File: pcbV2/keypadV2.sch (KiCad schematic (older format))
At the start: 74 parts, among them J1 Conn_01x02_Female, J2 USB_C_Receptacle, J3 Conn_01x03_Male, Q1 Q_NMOS_GSD, SW1 SW_Push, SW10 SW_Push, SW11 SW_Push, SW12 SW_Push, SW13 SW_SPDT, SW14 SW_Push, SW15 SW_Push, SW16 SW_Push, SW17 SW_DIP_x03, SW2 SW_Push, SW3 SW_Push, SW4 SW_Push, SW5 SW_Push, SW6 SW_Push, SW7 SW_Push, SW8 SW_Push, SW9 SW_Push, U1 Teensy4.0, U2 Waveshare_OLED_RGB

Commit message: .
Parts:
- added J6: Conn_01x03_Male, symbol Connector:Conn_01x03_Male
- J3: footprint Connector_PinHeader_2.00mm:PinHeader_1x03_P2.00mm_Vertical -> Connector_PinHeader_2.54mm:PinHeader_1x03_P2.54mm_Vertical
- R6: footprint (none) -> Resistor_SMD:R_1206_3216Metric_Pad1.42x1.75mm_HandSolder
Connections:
- net at D22.2 (DOUT): no longer D29.4 (DIN)
- new net RGB_UNDER: D29.4 (DIN), J6.2 (Pin_2)
- no-connect marks 45 -> 47
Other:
- moved on the sheet: C13, C14, C15, C16, D26, D27, D28, D29

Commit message: Start daughterboard
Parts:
- J6: footprint (none) -> Connector_PinSocket_2.54mm:PinSocket_1x03_P2.54mm_Vertical
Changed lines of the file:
@@
 F 0 "J6" H 8058 14631 50  0000 C CNN
 F 1 "Conn_01x03_Male" H 8058 14540 50  0000 C CNN
-F 2 "" H 7950 14350 50  0001 C CNN
+F 2 "Connector_PinSocket_2.54mm:PinSocket_1x03_P2.54mm_Vertical" H 7950 14350 50  0001 C CNN
 F 3 "~" H 7950 14350 50  0001 C CNN
 	1    7950 14350

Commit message: Updated schematic on mainboard, LEDs moved to daughter board
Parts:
- removed C1, C10, C11, C12, C2, C3, C4, C5, C6, C7, C8, C9: 1000uF, Capacitor_SMD:C_1206_3216Metric_Pad1.42x1.75mm_HandSolder, symbol Device:C
- removed D14, D15, D16, D17, D18, D19, D20, D21, D22, D23, D24, D25: WS2812B, LED_SMD:LED_WS2812B_PLCC4_5.0x5.0mm_P3.2mm, symbol LED:WS2812B
- removed R5: R_DIN, Resistor_SMD:R_1206_3216Metric_Pad1.42x1.75mm_HandSolder, symbol Device:R
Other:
- note added: "*Connect jumper to use 3.3V logic instead of the shifted 5V"
- note added: "Addressable RGBs"
- note added: "Keyboard Matrix"
- note added: "RGB Data Logic Level Shifter"
- note added: "RGB Daughter Board Connectors"
- note added: "Underglow RGB LEDs"
- note removed: "*Included extra 4 LEDs for underglow"
- note removed: "*Option to put 220-470ohm (close to DIN)"
- note removed: "*Use 3.3V logic instead of the shifted 5V"
- note removed: "Logic Level Shifter"
- note removed: "RGB Lighting"
- moved on the sheet: C13, C14, C15, C16, D13, D26, D27, D28, D29, J3, J6, Q1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

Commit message: Updated schematic to use seperate RGB Data pin for underglow LEDs
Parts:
- added H1, H2, H3, H4: MountingHole, MountingHole:MountingHole_3.2mm_M3, symbol Mechanical:MountingHole
- added Q2: Q_NMOS_GSD, Package_TO_SOT_SMD:SOT-23, symbol Device:Q_NMOS_GSD
- added R7: JUMPER, Resistor_SMD:R_1206_3216Metric_Pad1.42x1.75mm_HandSolder, symbol Device:R
- added R? (x2): 10K, Resistor_SMD:R_1206_3216Metric_Pad1.42x1.75mm_HandSolder, symbol Device:R
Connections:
- net +3V3: now also Q2.1 (G), R?.1
- net +5V: now also R?.1
- net BTN: now also U1.25 (18_A4_SDA0); no longer U1.21 (14_A0_TX3_SPDIF_OUT)
- net RGB_UNDER: now also Q2.3 (D), R7.1, R?.2; no longer J6.2 (Pin_2)
- net RGB_DATA renamed RGB_DATA1
- new net RGB_DATA2: Q2.2 (S), R7.2, R?.2, U1.21 (14_A0_TX3_SPDIF_OUT)
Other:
- note added: "*Empty connector used \nfor structural support"
- note added: "Mounting Holes"
- note added: "RGB Data Logic Level Shifter \n(Individual Backlighting)"
- note added: "RGB Data Logic Level Shifter \n(Underglow)"
- note removed: "RGB Data Logic Level Shifter"
- moved on the sheet: C13, C14, C15, C16, D26, D27, D28, D29, J3, J6

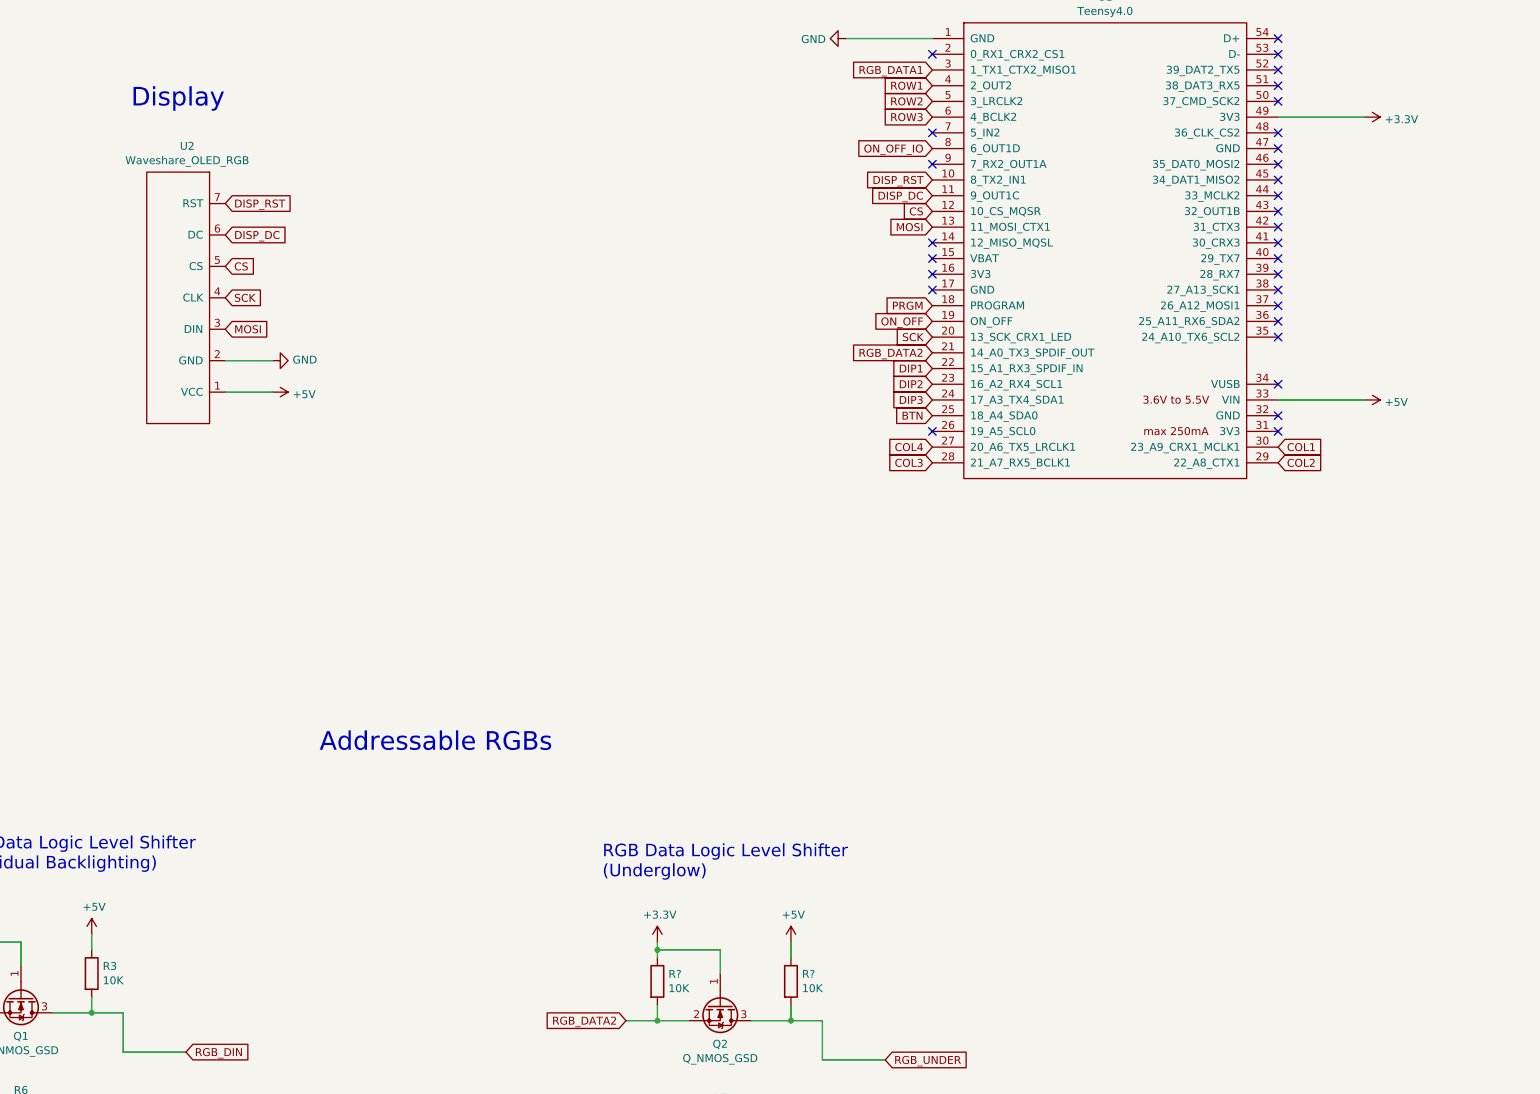
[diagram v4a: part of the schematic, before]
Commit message: 3.3V was on wrong pin on teens
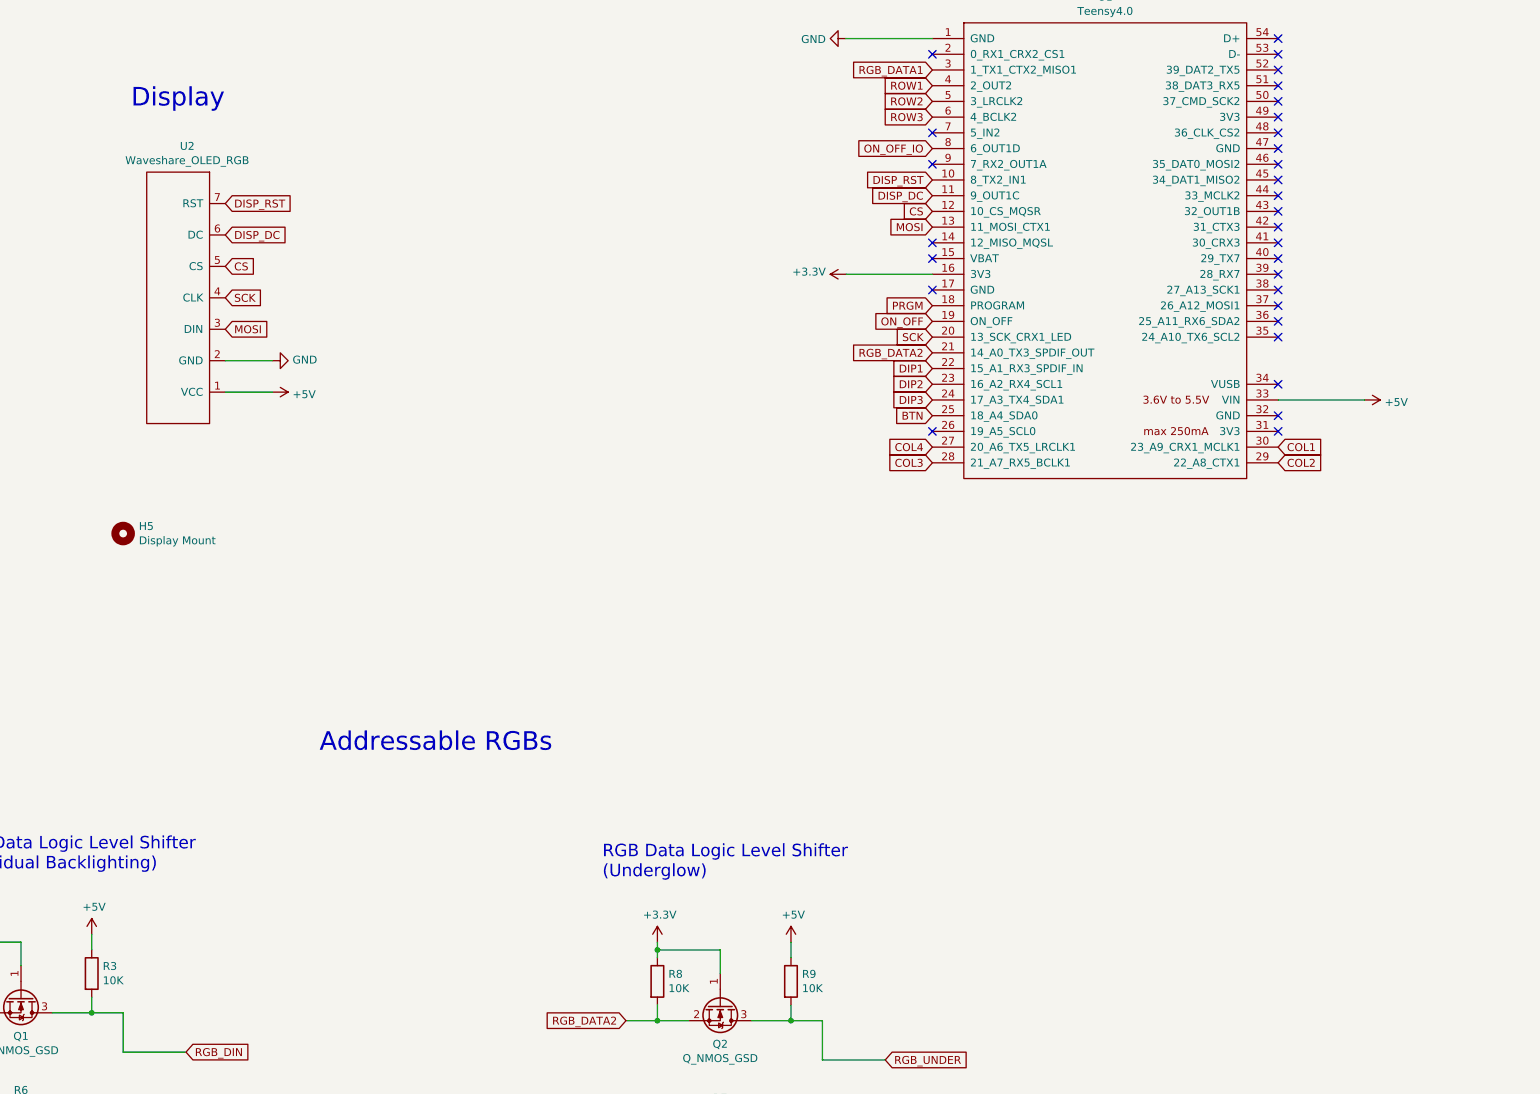
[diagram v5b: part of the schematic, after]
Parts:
- added H5: Display Mount, custom:Waveshare_LCD_mount V2, symbol Mechanical:MountingHole
- gave numbers to parts that had none: 2
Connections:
- net +3V3: now also U1.16 (3V3); no longer U1.49 (3V3)
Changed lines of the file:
@@
 L power:+3.3V #PWR0131
 U 1 1 5F108207
-P 11500 3550
-F 0 "#PWR0131" H 11500 3400 50  0001 C CNN
-F 1 "+3.3V" V 11515 3678 50  0000 L CNN
-F 2 "" H 11500 3550 50  0001 C CNN
-F 3 "" H 11500 3550 50  0001 C CNN
-	1    11500 3550
-	0    1    1    0
-$EndComp
-Wire Wire Line
-	11500 3550 10950 3550
+P 8200 4550
+F 0 "#PWR0131" H 8200 4400 50  0001 C CNN
+F 1 "+3.3V" V 8215 4678 50  0000 L CNN
+F 2 "" H 8200 4550 50  0001 C CNN
+F 3 "" H 8200 4550 50  0001 C CNN
+	1    8200 4550
+	0    -1   -1   0
+$EndComp
+Wire Wire Line
+	8200 4550 8750 4550
 Text GLabel 8750 4750 0    50   Input ~ 0
 PRGM
@@
 NoConn ~ 8750 4350
 NoConn ~ 8750 4450
-NoConn ~ 8750 4550
 NoConn ~ 8750 4650
 NoConn ~ 8750 5550
@@
 NoConn ~ 3000 11600
 $Comp
-L Device:R R?
+L Device:R R8
 U 1 1 5F102D2A
 P 7000 9050
-F 0 "R?" H 7070 9096 50  0000 L CNN
+F 0 "R8" H 7070 9096 50  0000 L CNN
 F 1 "10K" H 7070 9005 50  0000 L CNN
 F 2 "Resistor_SMD:R_1206_3216Metric_Pad1.42x1.75mm_HandSolder" V 6930 9050 50  0001 C CNN
@@
 $EndComp
 $Comp
-L Device:R R?
+L Device:R R9
 U 1 1 5F102D3F
 P 7850 9050
-F 0 "R?" H 7920 9096 50  0000 L CNN
+F 0 "R9" H 7920 9096 50  0000 L CNN
 F 1 "10K" H 7920 9005 50  0000 L CNN
 F 2 "Resistor_SMD:R_1206_3216Metric_Pad1.42x1.75mm_HandSolder" V 7780 9050 50  0001 C CNN
@@
 $EndComp
 $Comp
-L power:+3.3V #PWR?
+L power:+3.3V #PWR0101
 U 1 1 5F102D49
 P 7000 8800
-F 0 "#PWR?" H 7000 8650 50  0001 C CNN
+F 0 "#PWR0101" H 7000 8650 50  0001 C CNN
 F 1 "+3.3V" H 7015 8973 50  0000 C CNN
 F 2 "" H 7000 8800 50  0001 C CNN
@@
 $EndComp
 $Comp
-L power:+5V #PWR?
+L power:+5V #PWR0102
 U 1 1 5F102D53
 P 7850 8800
-F 0 "#PWR?" H 7850 8650 50  0001 C CNN
+F 0 "#PWR0102" H 7850 8650 50  0001 C CNN
 F 1 "+5V" H 7865 8973 50  0000 C CNN
 F 2 "" H 7850 8800 50  0001 C CNN
@@
 Text Notes 18300 6050 0    118  ~ 0
 Mounting Holes
+$Comp
+L Mechanical:MountingHole H5
+U 1 1 5F161619
+P 3600 6200
+F 0 "H5" H 3700 6246 50  0000 L CNN
+F 1 "Display Mount" H 3700 6155 50  0000 L CNN
+F 2 "custom:Waveshare_LCD_mount V2" H 3600 6200 50  0001 C CNN
+F 3 "~" H 3600 6200 50  0001 C CNN
+	1    3600 6200
+	1    0    0    -1
+$EndComp
+NoConn ~ 10950 3550
 $EndSCHEMATC

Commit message: Prototype 1 Code changes (#9)
* started working on low priority work thread

* removed usb c

* setup a low priority worker thread that we can assign a bunch of menial tasks to

* added dip switch support

* started rewiring

* v2 layout

* edited layout, updated daughter board

* moved some labels around

* generated plots files

* added the ability to enable, disable and delete threads by handler ID

* added thread safety to the low priority work thread

* added documentation for dip switches

* finished adding thread safety code, fixed SPI dma ram waste usage

* update

* updated gerber files

* moved over lpwork into it's own module

* added signature to the codebase

* added more signatures

* updating daughter board to be more structurally safe

* generated gerber files

Co-authored-by: Jonathan Low <jwlow@uci.edu>
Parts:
- removed J1: Conn_01x02_Female, Connector_PinHeader_2.00mm:PinHeader_1x02_P2.00mm_Vertical, symbol Connector:Conn_01x02_Female
- removed J2: USB_C_Receptacle, custom:USB_C_REDUCED_UJ31-CH-G2, symbol Connector:USB_C_Receptacle
- removed R4: R_SHIELD, Resistor_SMD:R_1206_3216Metric_Pad1.42x1.75mm_HandSolder, symbol Device:R
- removed SW13: SW_SPDT, Connector_PinHeader_2.54mm:PinHeader_1x03_P2.54mm_Vertical, symbol Switch:SW_SPDT
- C13, C14, C15, C16: value 1000uF -> 1uF
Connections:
- no-connect marks 47 -> 34
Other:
- note removed: "*Optional to connect shield to GND"
- note removed: "USB Data Breakouts"
- note removed: "USB-C Port"
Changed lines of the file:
@@
-$EndComp
-$Comp
-L Switch:SW_SPDT SW13
-U 1 1 5EF765BD
-P 13900 9000
-F 0 "SW13" H 13900 9285 50  0000 C CNN
-F 1 "SW_SPDT" H 13900 9194 50  0000 C CNN
-F 2 "Connector_PinHeader_2.54mm:PinHeader_1x03_P2.54mm_Vertical" H 13900 9000 50  0001 C CNN
-F 3 "~" H 13900 9000 50  0001 C CNN
-	1    13900 9000
-	1    0    0    -1
 $EndComp
 $Comp
@@
 $EndComp
 $Comp
-L Connector:USB_C_Receptacle J2
-U 1 1 5EF7AA75
-P 18650 11500
-F 0 "J2" H 18220 11197 50  0000 R CNN
-F 1 "USB_C_Receptacle" H 18220 11288 50  0000 R CNN
-F 2 "custom:USB_C_REDUCED_UJ31-CH-G2" H 18800 11500 50  0001 C CNN
-F 3 "https://www.usb.org/sites/default/files/documents/usb_type-c.zip" H 18800 11500 50  0001 C CNN
-	1    18650 11500
-	-1   0    0    1
-$EndComp
-$Comp
 L Switch:SW_DIP_x03 SW17
 U 1 1 5EF7EA1C
@@
 P 5050 11800
 F 0 "C13" H 5165 11846 50  0000 L CNN
-F 1 "1000uF" H 5165 11755 50  0000 L CNN
+F 1 "1uF" H 5165 11755 50  0000 L CNN
 F 2 "Capacitor_SMD:C_1206_3216Metric_Pad1.42x1.75mm_HandSolder" H 5088 11650 50  0001 C CNN
 F 3 "~" H 5050 11800 50  0001 C CNN
@@
 P 6050 11800
 F 0 "C14" H 6165 11846 50  0000 L CNN
-F 1 "1000uF" H 6165 11755 50  0000 L CNN
+F 1 "1uF" H 6165 11755 50  0000 L CNN
 F 2 "Capacitor_SMD:C_1206_3216Metric_Pad1.42x1.75mm_HandSolder" H 6088 11650 50  0001 C CNN
 F 3 "~" H 6050 11800 50  0001 C CNN
@@
 P 7050 11800
 F 0 "C15" H 7165 11846 50  0000 L CNN
-F 1 "1000uF" H 7165 11755 50  0000 L CNN
+F 1 "1uF" H 7165 11755 50  0000 L CNN
 F 2 "Capacitor_SMD:C_1206_3216Metric_Pad1.42x1.75mm_HandSolder" H 7088 11650 50  0001 C CNN
 F 3 "~" H 7050 11800 50  0001 C CNN
@@
 P 8050 11800
 F 0 "C16" H 8165 11846 50  0000 L CNN
-F 1 "1000uF" H 8165 11755 50  0000 L CNN
+F 1 "1uF" H 8165 11755 50  0000 L CNN
 F 2 "Capacitor_SMD:C_1206_3216Metric_Pad1.42x1.75mm_HandSolder" H 8088 11650 50  0001 C CNN
 F 3 "~" H 8050 11800 50  0001 C CNN
@@
 	0    1    1    0
 $EndComp
-NoConn ~ 18050 10200
-NoConn ~ 18050 10300
-$Comp
-L Device:R R4
-U 1 1 5F08CE6B
-P 19400 9600
-F 0 "R4" V 19193 9600 50  0000 C CNN
-F 1 "R_SHIELD" V 19284 9600 50  0000 C CNN
-F 2 "Resistor_SMD:R_1206_3216Metric_Pad1.42x1.75mm_HandSolder" V 19330 9600 50  0001 C CNN
-F 3 "~" H 19400 9600 50  0001 C CNN
-	1    19400 9600
-	0    1    1    0
-$EndComp
-Wire Wire Line
-	19250 9600 18950 9600
-Wire Wire Line
-	18950 9600 18950 9900
-$Comp
-L power:GND #PWR0125
-U 1 1 5F092F41
-P 18650 9600
-F 0 "#PWR0125" H 18650 9350 50  0001 C CNN
-F 1 "GND" H 18655 9427 50  0000 C CNN
-F 2 "" H 18650 9600 50  0001 C CNN
-F 3 "" H 18650 9600 50  0001 C CNN
-	1    18650 9600
-	-1   0    0    1
-$EndComp
-Wire Wire Line
-	18650 9900 18650 9600
-NoConn ~ 18050 11400
-NoConn ~ 18050 11500
-NoConn ~ 18050 11100
-NoConn ~ 18050 11200
-NoConn ~ 18050 10800
-NoConn ~ 18050 10900
-NoConn ~ 18050 10500
-NoConn ~ 18050 10600
-NoConn ~ 18050 12200
-NoConn ~ 18050 12300
-$Comp
-L power:GND #PWR0126
-U 1 1 5F0BF5B3
-P 19750 9600
-F 0 "#PWR0126" H 19750 9350 50  0001 C CNN
-F 1 "GND" H 19755 9427 50  0000 C CNN
-F 2 "" H 19750 9600 50  0001 C CNN
-F 3 "" H 19750 9600 50  0001 C CNN
-	1    19750 9600
-	-1   0    0    1
-$EndComp
-Wire Wire Line
-	19750 9600 19550 9600
-Text GLabel 17800 11700 0    50   Input ~ 0
-USB_DATA+
-Text GLabel 17800 11800 0    50   Input ~ 0
-USB_DATA+
-Text GLabel 17800 11900 0    50   Input ~ 0
-USB_DATA-
-Text GLabel 17800 12000 0    50   Input ~ 0
-USB_DATA-
-Text GLabel 17800 12500 0    50   Input ~ 0
-USB_VBUS
-Wire Wire Line
-	18050 11700 17800 11700
-Wire Wire Line
-	18050 11800 17800 11800
-Wire Wire Line
-	18050 11900 17800 11900
-Wire Wire Line
-	18050 12000 17800 12000
-Wire Wire Line
-	18050 12500 17800 12500
-Text Notes 19250 9850 0    50   ~ 0
-*Optional to connect shield to GND
-Wire Wire Line
-	14100 8900 14400 8900
-$Comp
-L power:+5V #PWR0127
-U 1 1 5F0D8397
-P 14400 8900
-F 0 "#PWR0127" H 14400 8750 50  0001 C CNN
-F 1 "+5V" V 14415 9028 50  0000 L CNN
-F 2 "" H 14400 8900 50  0001 C CNN
-F 3 "" H 14400 8900 50  0001 C CNN
-	1    14400 8900
-	0    1    1    0
-$EndComp
-Wire Wire Line
-	13700 9000 13550 9000
-Text GLabel 13550 9000 0    50   Input ~ 0
-USB_VBUS
 Text GLabel 8750 4850 0    50   Input ~ 0
 ON_OFF
@@
 	3600 9250 3400 9250
 Connection ~ 3400 9250
-$Comp
-L Connector:Conn_01x02_Female J1
-U 1 1 5F17D824
-P 18550 7900
-F 0 "J1" H 18578 7876 50  0000 L CNN
-F 1 "Conn_01x02_Female" H 18578 7785 50  0000 L CNN
-F 2 "Connector_PinHeader_2.00mm:PinHeader_1x02_P2.00mm_Vertical" H 18550 7900 50  0001 C CNN
-F 3 "~" H 18550 7900 50  0001 C CNN
-	1    18550 7900
-	1    0    0    -1
-$EndComp
-Text GLabel 18200 7900 0    50   Input ~ 0
-USB_DATA+
-Text GLabel 18200 8000 0    50   Input ~ 0
-USB_DATA-
-Wire Wire Line
-	18350 7900 18200 7900
-Wire Wire Line
-	18350 8000 18200 8000
 Wire Wire Line
 	5650 11350 6050 11350
@@
 Text Notes 13300 8400 0    118  ~ 0
 Power Controls
-Text Notes 17650 7650 0    118  ~ 0
-USB Data Breakouts
 Text Notes 3650 3500 0    118  ~ 0
 Display
 Text Notes 4850 7600 0    118  ~ 0
 Addressable RGBs
-Text Notes 18050 9100 0    118  ~ 0
-USB-C Port
 Text Notes 2500 8350 0    79   ~ 0
 RGB Data Logic Level Shifter \n(Individual Backlighting)
@@
 $EndComp
 NoConn ~ 5050 11350
-NoConn ~ 14100 9100
 Text GLabel 3000 11050 2    50   Input ~ 0
 RGB_DIN
